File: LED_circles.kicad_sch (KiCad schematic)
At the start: 6 parts

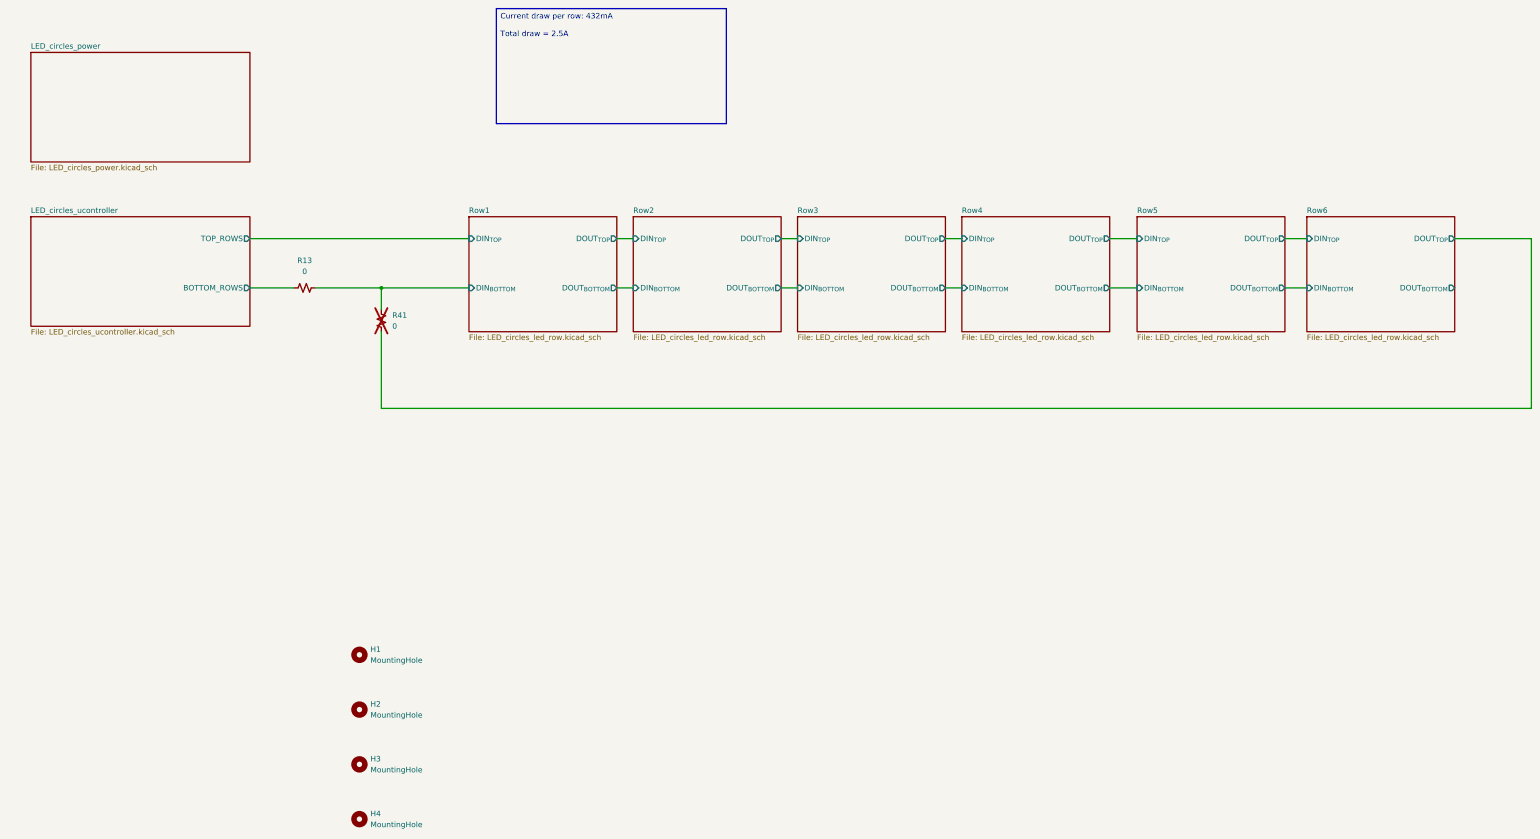
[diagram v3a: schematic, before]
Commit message: Deleted parts not used in single row test PCB
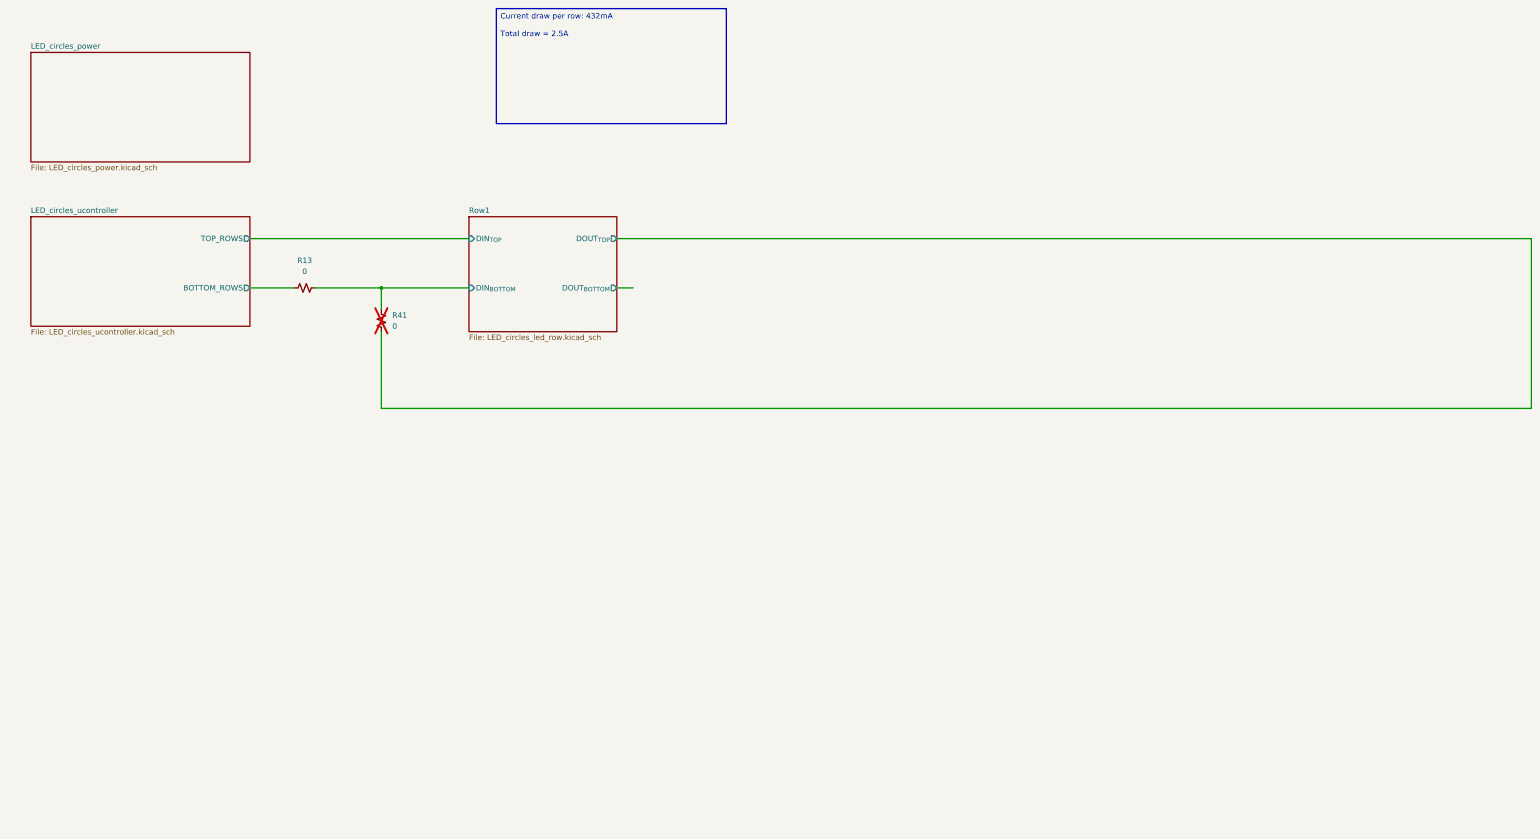
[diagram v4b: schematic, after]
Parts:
- removed H1, H2, H3, H4: MountingHole, MountingHole:MountingHole_2.5mm, symbol Mechanical:MountingHole
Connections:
- net Row6/DOUT_{TOP} is gone; now on net Row1/DOUT_{TOP}: R41.2
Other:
- removed sheet Row2
- removed sheet Row3
- removed sheet Row4
- removed sheet Row5
- removed sheet Row6

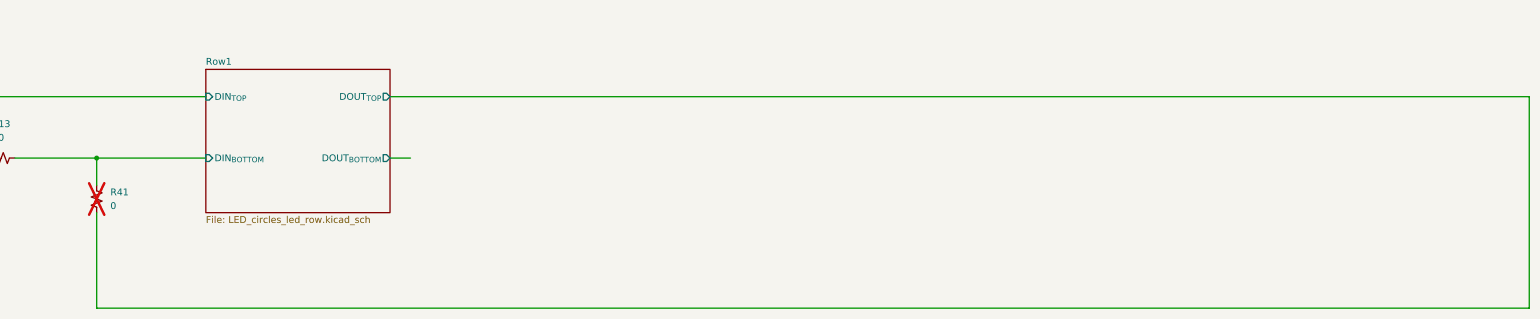
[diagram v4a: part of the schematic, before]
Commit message: Made vias really big so one can make them on a circuit mill
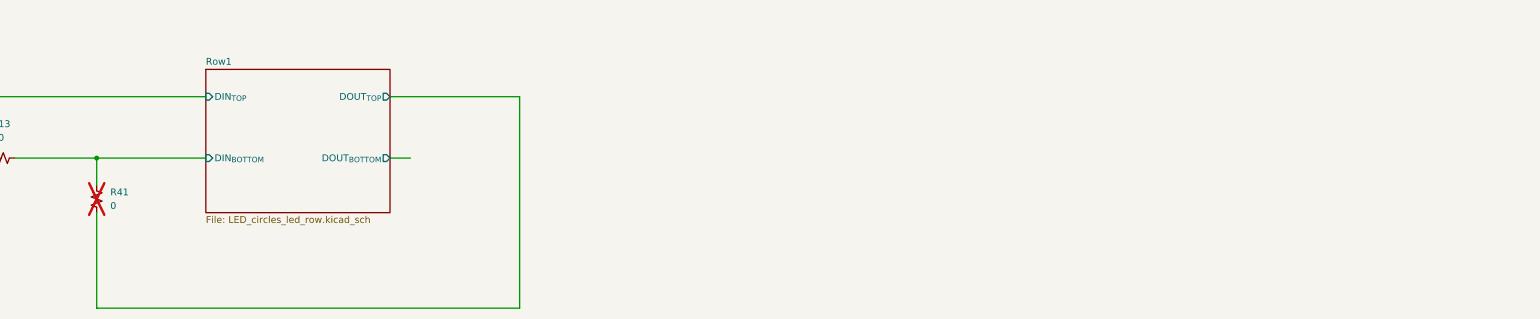
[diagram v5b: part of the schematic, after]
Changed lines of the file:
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@@
 	(wire
 		(pts
-			(xy 373.38 93.98) (xy 373.38 133.35)
+			(xy 185.42 93.98) (xy 185.42 133.35)
 		)
 		(stroke
@@
 	(wire
 		(pts
-			(xy 373.38 133.35) (xy 106.68 133.35)
+			(xy 185.42 133.35) (xy 106.68 133.35)
 		)
 		(stroke
@@
 	(wire
 		(pts
-			(xy 161.29 93.98) (xy 373.38 93.98)
+			(xy 161.29 93.98) (xy 185.42 93.98)
 		)
 		(stroke
